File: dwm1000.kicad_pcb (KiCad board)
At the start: 2 copper layers, 38.8 x 29.5 mm, 19 parts, among them J1 CONN_01X02, J10 CONN_01X08, J11 CONN_01X05, J12 CONN_01X05, J2 CONN_01X05, J3 CONN_01X05, J4 CONN_01X14, J5 CONN_01X14, J6 CONN_01X02, J7 CONN_01X02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

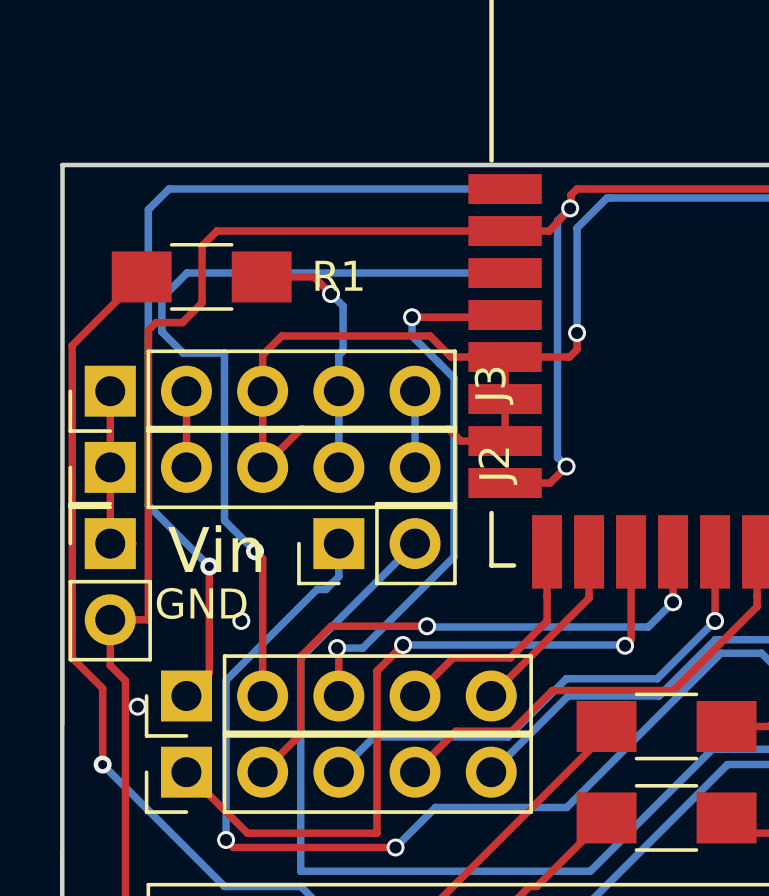
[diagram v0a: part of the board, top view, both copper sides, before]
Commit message: correction of 2 missing connections on DW1000
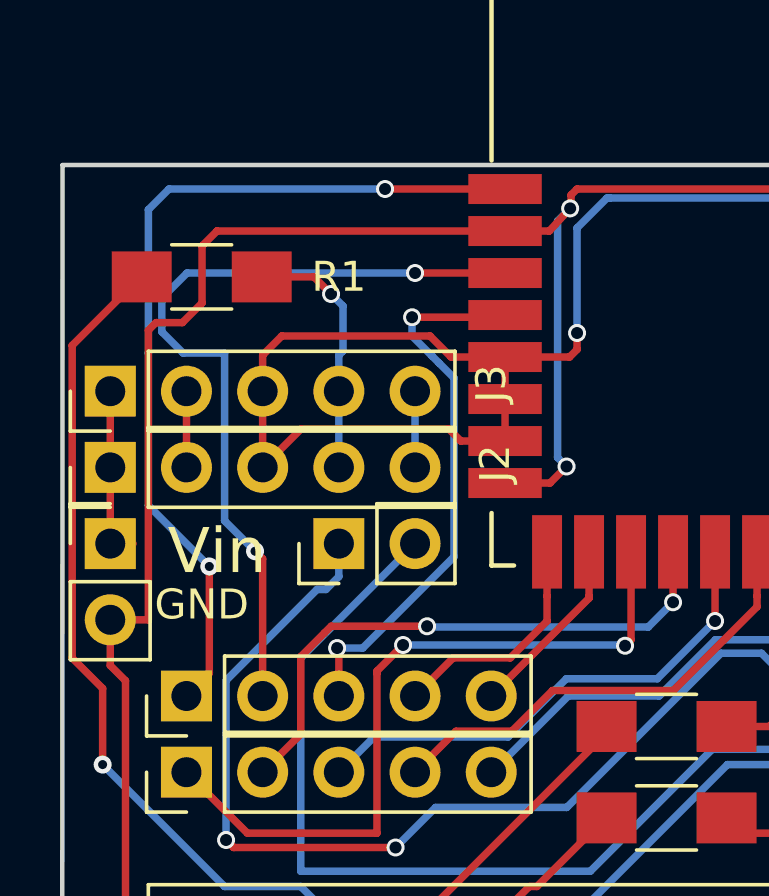
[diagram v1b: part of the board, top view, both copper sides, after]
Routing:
- net EXTON: vias 1 -> 2
- net RSTn: vias 1 -> 2
- net GND: vias 6 -> 4
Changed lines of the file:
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@@
     (thickness 1.6)
     (drawings 20)
-    (tracks 337)
+    (tracks 341)
     (zones 0)
     (modules 19)
@@
   (segment (start 172.942 92.456) (end 174.371 92.456) (width 0.25) (layer F.Cu) (net 3))
   (via (at 174.879 91.948) (size 0.6) (drill 0.4) (layers F.Cu B.Cu) (net 3))
-  (via (at 156.7688 88.9381) (size 0.6) (drill 0.4) (layers F.Cu B.Cu) (net 4))
-  (via (at 153.3144 91.7956) (size 0.6) (drill 0.4) (layers F.Cu B.Cu) (net 4))
   (segment (start 159.290998 87.89) (end 159.59 87.89) (width 0.25) (layer B.Cu) (net 5))
   (segment (start 160.02 87.46) (end 160.02 86.36) (width 0.25) (layer B.Cu) (net 5))
@@
   (segment (start 173.482 96.012) (end 172.974 95.504) (width 0.25) (layer F.Cu) (net 2) (status 80030))
   (segment (start 172.974 95.504) (end 172.942 95.504) (width 0.25) (layer F.Cu) (net 2) (status 80030))
+  (segment (start 162.56 77.34) (end 165.5588 77.34) (width 0.25) (layer F.Cu) (net 36))
+  (segment (start 165.5588 77.34) (end 165.56 77.3412) (width 0.25) (layer F.Cu) (net 36))
+  (segment (start 154.96 77.34) (end 162.56 77.34) (width 0.25) (layer B.Cu) (net 36))
+  (via (at 162.56 77.34) (size 0.6) (drill 0.4) (layers F.Cu B.Cu) (net 36))
+  (segment (start 161.56 74.54) (end 165.5588 74.54) (width 0.25) (layer F.Cu) (net 37))
+  (segment (start 165.5588 74.54) (end 165.56 74.5412) (width 0.25) (layer F.Cu) (net 37))
+  (via (at 161.56 74.54) (size 0.6) (drill 0.4) (layers F.Cu B.Cu) (net 37))
+  (segment (start 154.36 74.54) (end 161.56 74.54) (width 0.25) (layer B.Cu) (net 37))
   (segment (start 182.372 85.702) (end 181.6318 84.9618) (width 0.25) (layer F.Cu) (net 38))
   (segment (start 182.372 87.408) (end 182.372 85.702) (width 0.25) (layer F.Cu) (net 38))
@@
   (segment (start 160.02 91.44) (end 160.02 89.9) (width 0.25) (layer F.Cu) (net 35))
   (via (at 159.961942 89.841942) (size 0.6) (drill 0.4) (layers F.Cu B.Cu) (net 35))
-  (segment (start 154.96 77.34) (end 165.56 77.34) (width 0.25) (layer B.Cu) (net 36))
   (segment (start 154.12001 78.17999) (end 154.96 77.34) (width 0.25) (layer B.Cu) (net 36))
   (segment (start 154.12001 79.30001) (end 154.12001 78.17999) (width 0.25) (layer B.Cu) (net 36))
@@
   (segment (start 157.226 86.614) (end 157.48 86.868) (width 0.25) (layer F.Cu) (net 36) (status 80000))
   (segment (start 157.48 86.868) (end 157.48 91.44) (width 0.25) (layer F.Cu) (net 36) (status 80020))
-  (segment (start 154.36 74.54) (end 165.56 74.54) (width 0.25) (layer B.Cu) (net 37))
   (segment (start 153.67 75.23) (end 154.36 74.54) (width 0.25) (layer B.Cu) (net 37))
   (segment (start 153.67 80.01) (end 153.67 75.23) (width 0.25) (layer B.Cu) (net 37))

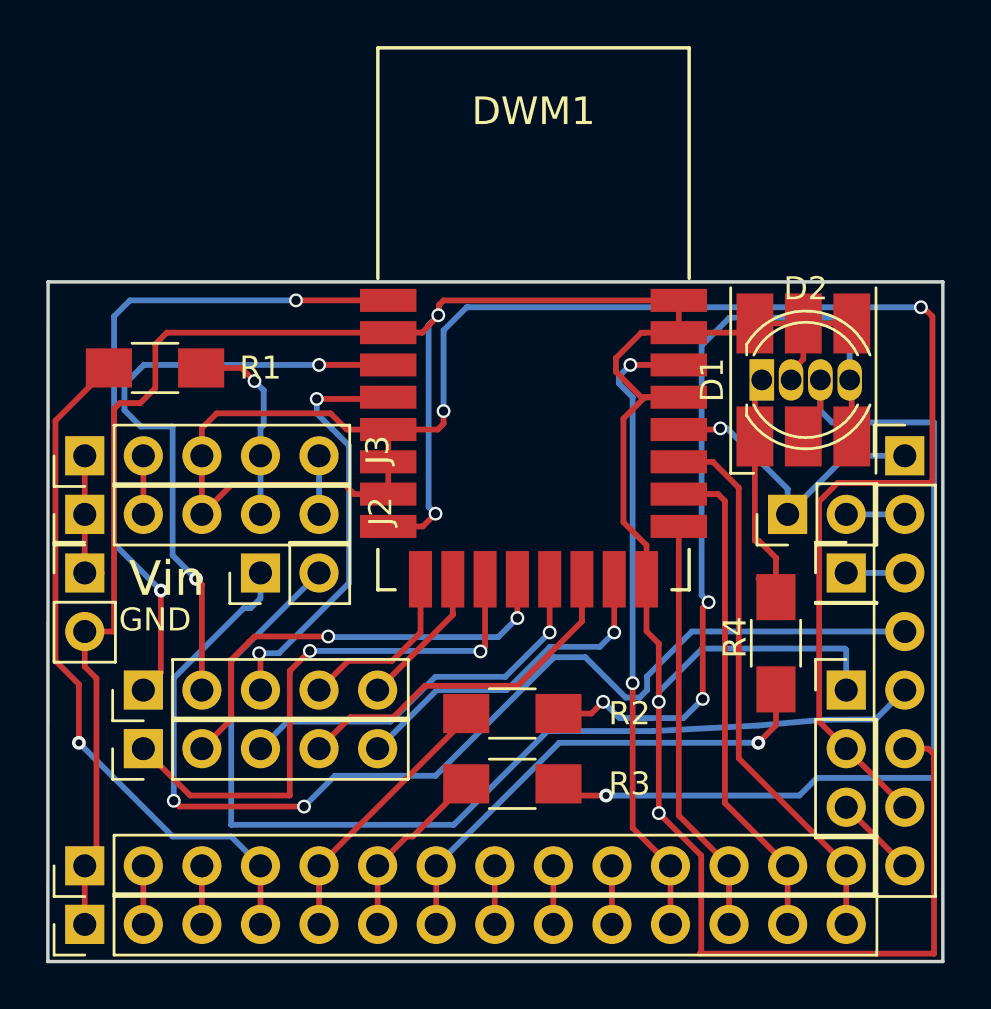
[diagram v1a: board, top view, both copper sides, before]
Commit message: adding ground planes both sides
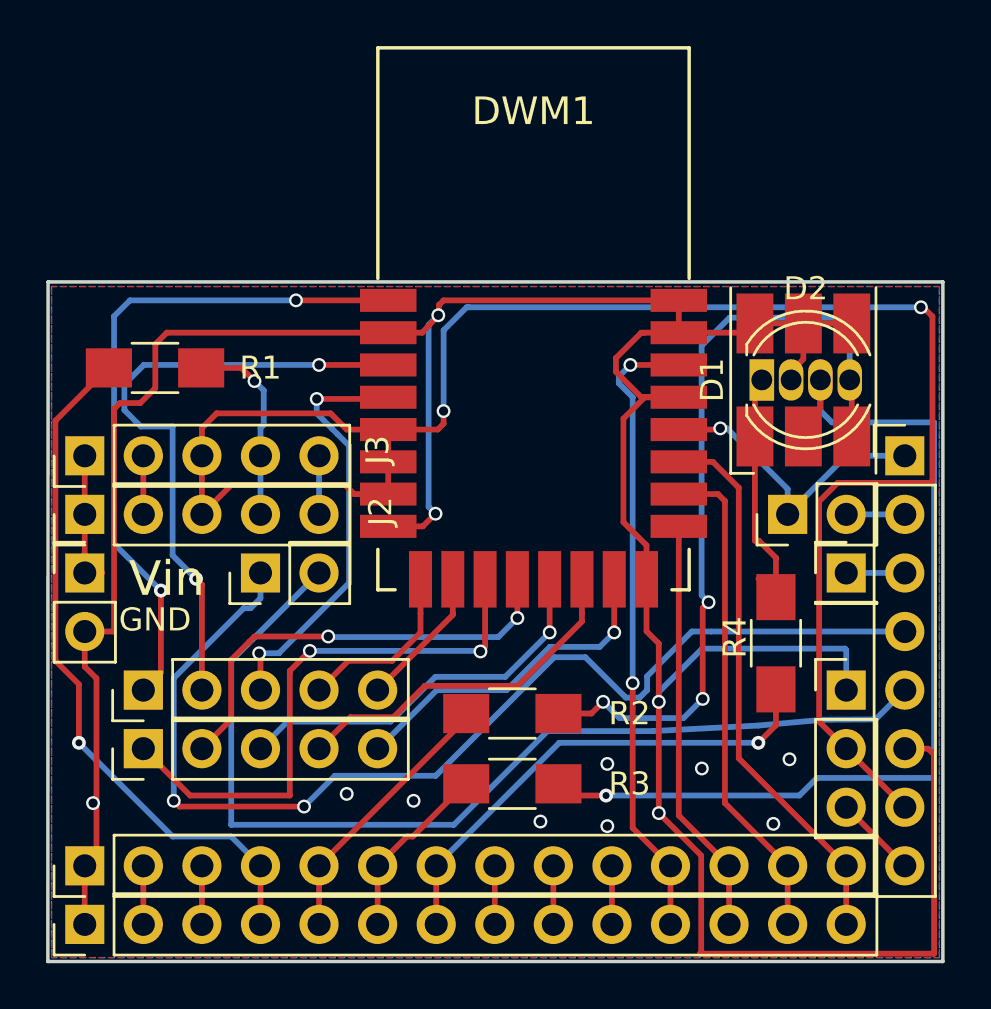
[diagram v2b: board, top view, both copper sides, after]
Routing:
- net GND: vias 4 -> 12
- net (no net): vias 0 -> 1
- added copper zone on B.Cu, net GND
- added copper zone on F.Cu, net GND
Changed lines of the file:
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@@
     (thickness 1.6)
     (drawings 20)
-    (tracks 341)
+    (tracks 350)
     (zones 0)
     (modules 19)
@@
   )
   (gr_line (start 150.81 73.74) (end 189.61 73.74) (angle 90) (layer Edge.Cuts) (width 0.15))
+  (via (at 166.66 96.24) (size 0.6) (drill 0.4) (layers F.Cu B.Cu) (net 0))
   (segment (start 167.96 79.89) (end 167.7088 80.1412) (width 0.25) (layer F.Cu) (net 1))
   (segment (start 167.96 79.34) (end 167.96 79.89) (width 0.25) (layer F.Cu) (net 1))
@@
   (segment (start 185.66 80.44) (end 185.66 78.08) (width 0.25) (layer F.Cu) (net 3))
   (segment (start 185.66 78.08) (end 185.57 77.99) (width 0.25) (layer F.Cu) (net 3))
+  (via (at 175.06 94.64) (size 0.6) (drill 0.4) (layers F.Cu B.Cu) (net 4))
+  (via (at 179.16 94.84) (size 0.6) (drill 0.4) (layers F.Cu B.Cu) (net 4))
+  (via (at 163.76 95.94) (size 0.6) (drill 0.4) (layers F.Cu B.Cu) (net 4))
+  (via (at 152.76 96.34) (size 0.6) (drill 0.4) (layers F.Cu B.Cu) (net 4))
+  (via (at 172.16 97.14) (size 0.6) (drill 0.4) (layers F.Cu B.Cu) (net 4))
+  (via (at 175.06 97.34) (size 0.6) (drill 0.4) (layers F.Cu B.Cu) (net 4))
+  (via (at 182.26 97.24) (size 0.6) (drill 0.4) (layers F.Cu B.Cu) (net 4))
+  (via (at 182.96 94.44) (size 0.6) (drill 0.4) (layers F.Cu B.Cu) (net 4))
   (segment (start 178.16 75.9412) (end 181.0588 75.9412) (width 0.25) (layer F.Cu) (net 4))
   (segment (start 181.0588 75.9412) (end 181.46 75.54) (width 0.25) (layer F.Cu) (net 4))
@@
   (segment (start 155.702 87.122) (end 153.67 85.09) (width 0.25) (layer B.Cu) (net 37) (status 80000))
   (segment (start 153.67 85.09) (end 153.67 80.01) (width 0.25) (layer B.Cu) (net 37) (status 80000))
+  (zone (net 4) (net_name GND) (layer F.Cu) (hatch edge 0.508)
+    (connect_pads (clearance 0.508))
+    (min_thickness 0.254)
+    (fill yes (arc_segments 16) (thermal_gap 0.508) (thermal_bridge_width 0.508))
+    (polygon
+      (pts
+        (xy 150.96 103.04) (xy 150.96 73.94) (xy 189.46 73.94) (xy 189.46 103.04)
+      )
+    )
+  )
+  (zone (net 4) (net_name GND) (layer B.Cu) (hatch edge 0.508)
+    (connect_pads (clearance 0.508))
+    (min_thickness 0.254)
+    (fill yes (arc_segments 16) (thermal_gap 0.508) (thermal_bridge_width 0.508))
+    (polygon
+      (pts
+        (xy 189.46 73.94) (xy 150.96 73.94) (xy 150.96 103.04) (xy 189.46 103.04)
+      )
+    )
+  )
 )
